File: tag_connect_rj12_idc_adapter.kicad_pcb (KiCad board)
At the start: 2 copper layers, 30 x 16 mm, 2 parts, among them CON1 AVR-ISP-6, J1 RJ12

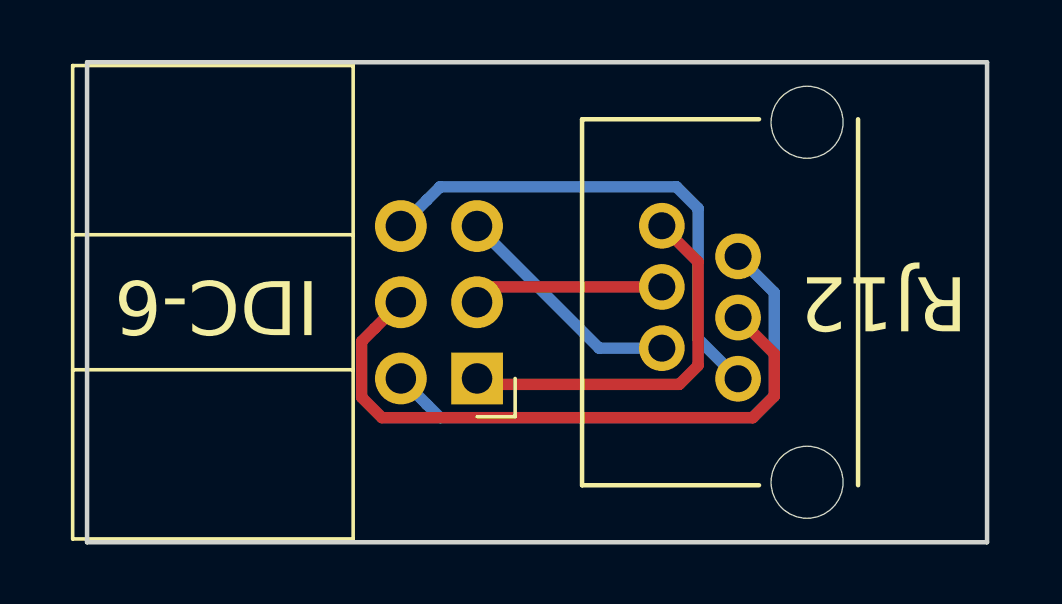
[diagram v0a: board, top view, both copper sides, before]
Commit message: order of IDC pins was reversed
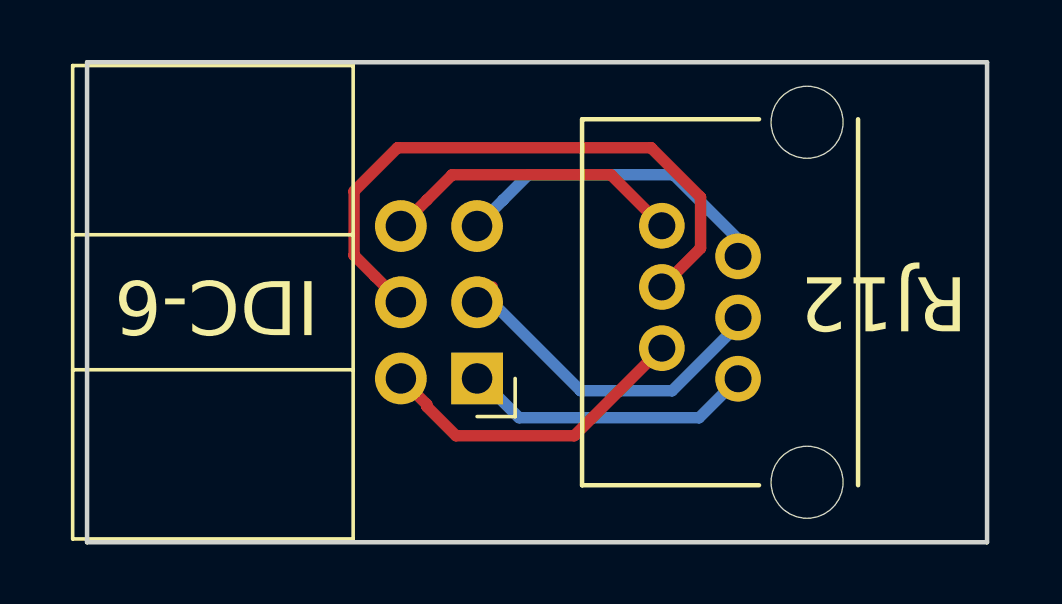
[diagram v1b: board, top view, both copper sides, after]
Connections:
- CON1 pad 1: /IDC-6 -> /IDC-1
- CON1 pad 2: /IDC-5 -> /IDC-2
- CON1 pad 3: /IDC-4 -> /IDC-3
- CON1 pad 4: /IDC-3 -> /IDC-4
- CON1 pad 5: /IDC-2 -> /IDC-5
- CON1 pad 6: /IDC-1 -> /IDC-6
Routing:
- net /IDC-4: track 6.37 -> 20.7 mm
- net /IDC-3: track 21.2 -> 12.1 mm
- net /IDC-5: track 18.4 -> 10.9 mm
- net /IDC-1: track 17.0 -> 10.1 mm
- net /IDC-2: track 7.85 -> 10.7 mm
- net /IDC-6: track 12.9 -> 10.1 mm
